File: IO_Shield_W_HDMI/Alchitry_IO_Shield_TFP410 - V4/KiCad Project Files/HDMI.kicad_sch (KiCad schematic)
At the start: 19 parts, among them J0 HDMI_A_1.4, U1 TFP410

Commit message: minor changes
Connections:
- net +3V3: now also J0.18 (+5V), JP0.2 (C)

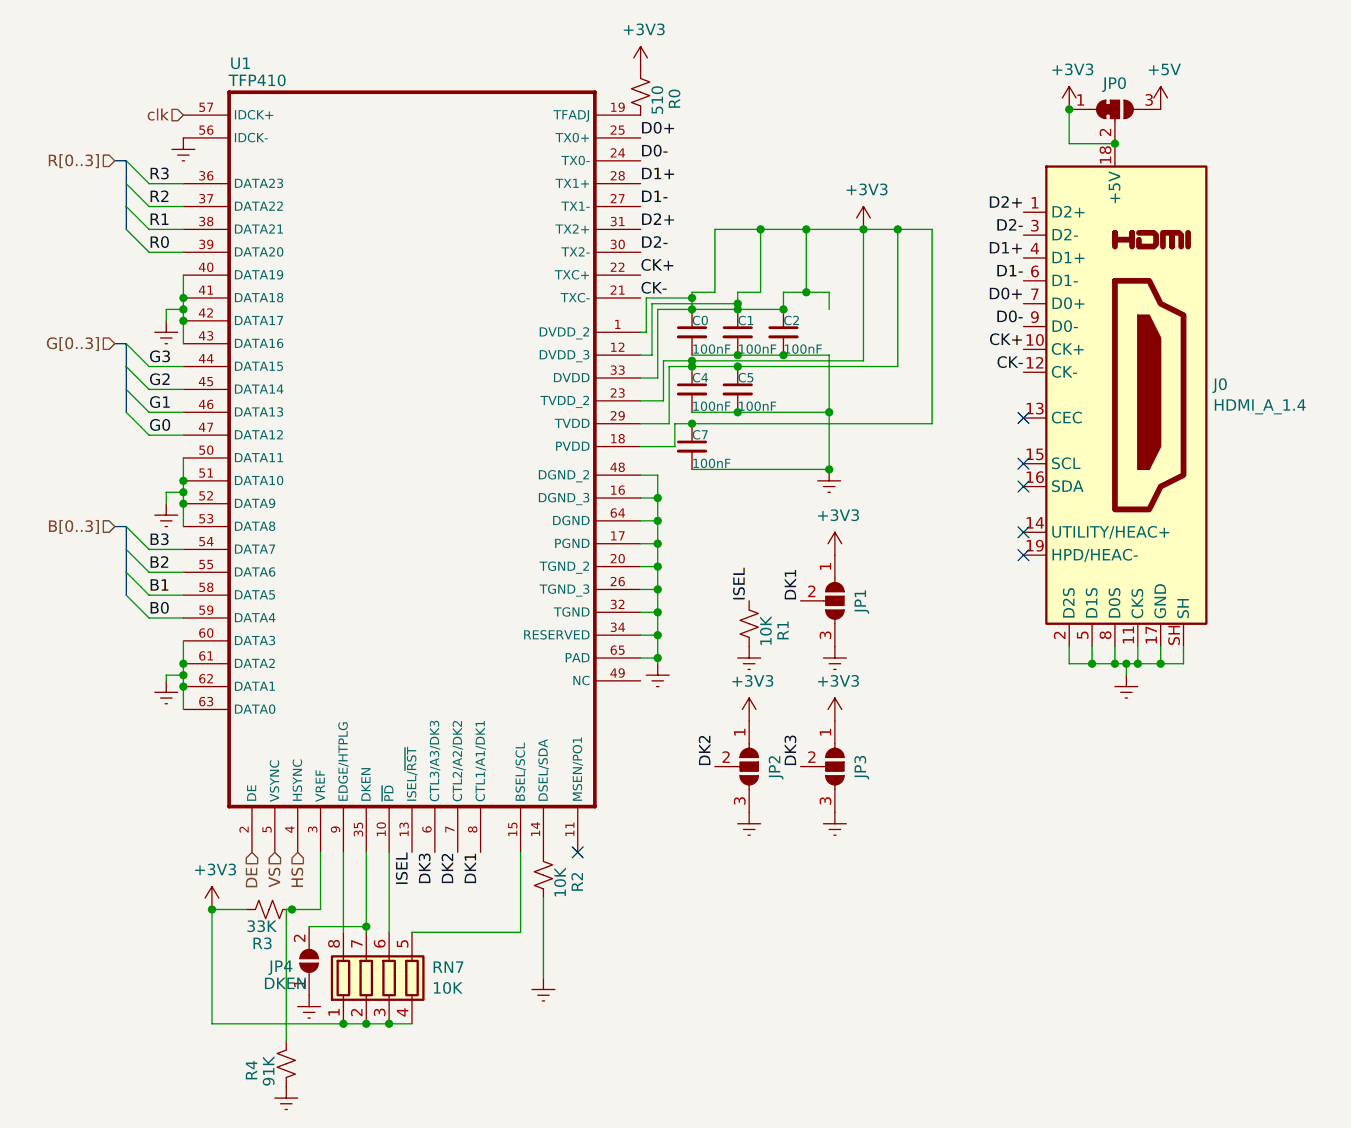
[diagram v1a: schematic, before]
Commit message: updated shield v4 schematic
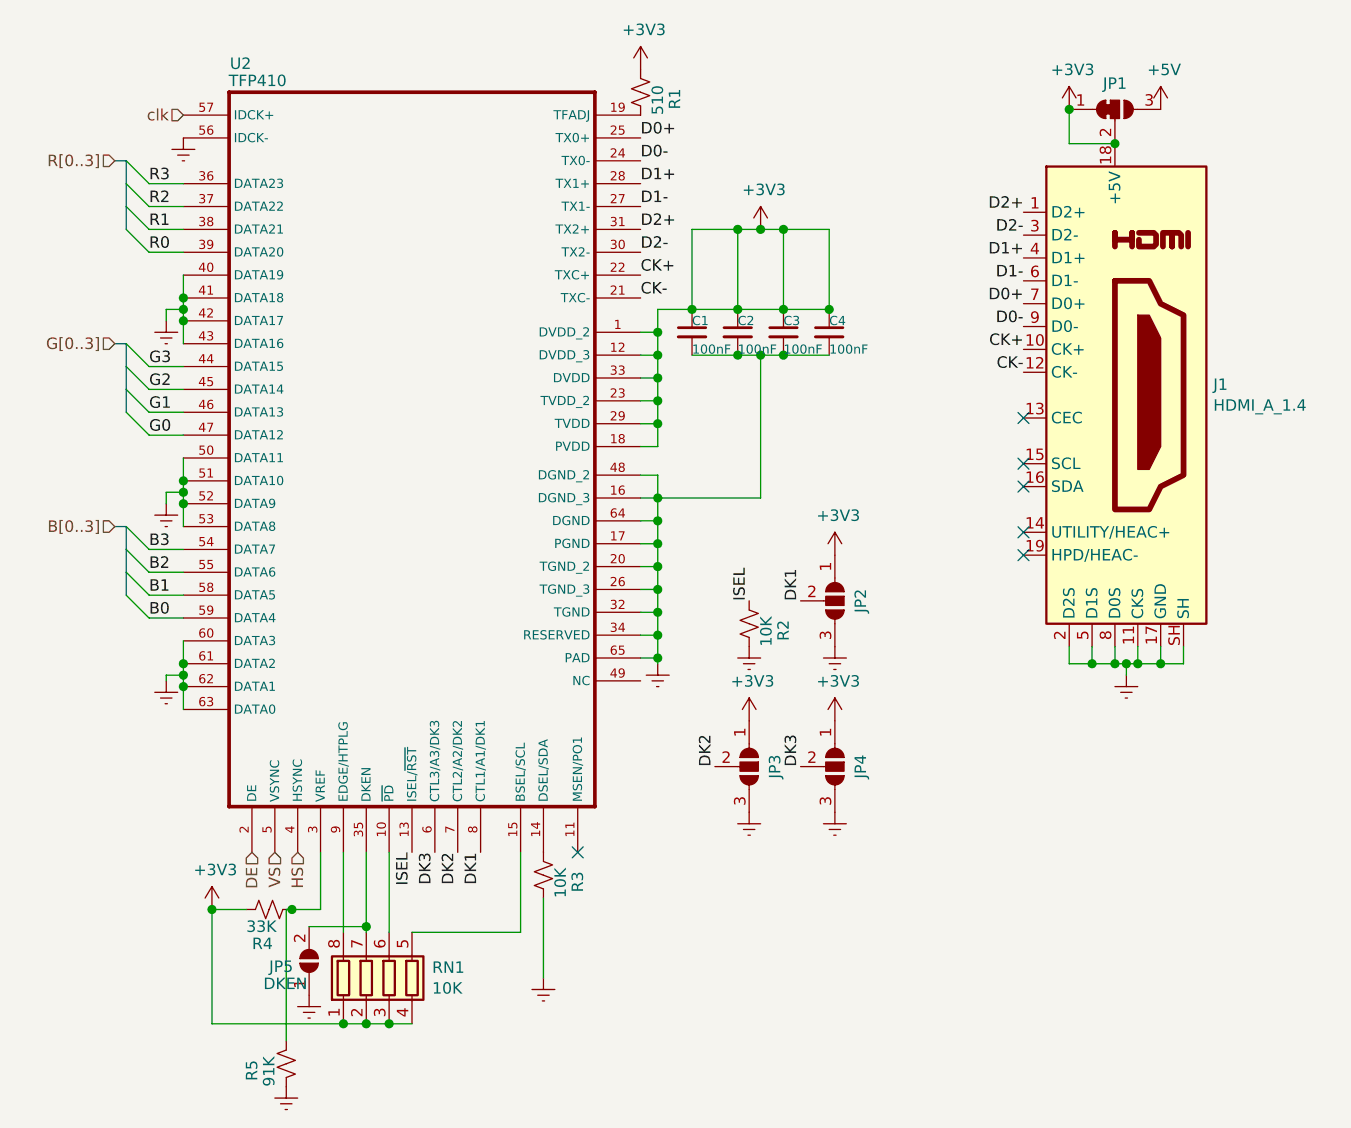
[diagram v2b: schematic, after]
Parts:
- removed C4, C5: 100nF, Capacitor_SMD:C_0603_1608Metric_Pad1.05x0.95mm_HandSolder, symbol Device:C_Small
- C1: renamed from C0; footprint Capacitor_SMD:C_0603_1608Metric_Pad1.05x0.95mm_HandSolder -> Capacitor_SMD:C_0603_1608Metric
- C2: renamed from C1; footprint Capacitor_SMD:C_0603_1608Metric_Pad1.05x0.95mm_HandSolder -> Capacitor_SMD:C_0603_1608Metric
- C3: renamed from C2; footprint Capacitor_SMD:C_0603_1608Metric_Pad1.05x0.95mm_HandSolder -> Capacitor_SMD:C_0603_1608Metric
- C4: renamed from C7; footprint Capacitor_SMD:C_0603_1608Metric_Pad1.05x0.95mm_HandSolder -> Capacitor_SMD:C_0603_1608Metric
- R1: renamed from R0; footprint Resistor_SMD:R_0603_1608Metric_Pad1.05x0.95mm_HandSolder -> Resistor_SMD:R_0603_1608Metric
- renumbered J0 to J1, JP0 to JP1, JP1 to JP2, JP2 to JP3, JP3 to JP4, JP4 to JP5, R1 to R2, R2 to R3, R3 to R4, R4 to R5, RN7 to RN1, U1 to U2
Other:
- moved on the sheet: C4
